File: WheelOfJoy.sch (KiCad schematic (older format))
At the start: 39 parts, among them CN1 JOY1, CN2 JOY2, CN3 JOY3, CN4 JOY4, CN5 JOY5, CN6 JOY6, CN7 JOY7, CN8 JOY8, CN9 DB15F, U1 CD4051B, U2 CD4051B, U3 CD4051B, U4 CD4051B, U5 CD4051B

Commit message: WIP
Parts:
- removed C4, C5: 100n, Capacitor_THT:C_Disc_D7.0mm_W2.5mm_P5.00mm, symbol Device:C
- removed CN5: JOY5, Connector_Dsub:DSUB-9_Male_EdgeMount_P2.77mm, symbol Connector:DB9_Male_MountingHoles
- removed CN6: JOY6, Connector_Dsub:DSUB-9_Male_EdgeMount_P2.77mm, symbol Connector:DB9_Male_MountingHoles
- removed CN7: JOY7, Connector_Dsub:DSUB-9_Male_EdgeMount_P2.77mm, symbol Connector:DB9_Male_MountingHoles
- removed CN8: JOY8, Connector_Dsub:DSUB-9_Male_EdgeMount_P2.77mm, symbol Connector:DB9_Male_MountingHoles
- removed RN1, RN2, RN3, RN4, RN5, RN6, RN7, RN8: 4.7k, Resistor_THT:R_Array_SIP6, symbol Device:R_Network05
- removed RN9: 100, Resistor_THT:R_Array_SIP10, symbol Device:R_Pack05_SIP_Split
- removed U1, U2, U3, U4, U5: CD4051B, Package_DIP:DIP-16_W7.62mm_Socket_LongPads, symbol Analog_Switch:CD4051B
- removed V6: PORT5_NO, WheelOfJoy:port5, symbol void:Void
- removed V7: PORT6_NO, WheelOfJoy:port6, symbol void:Void
- removed V8: PORT7_NO, WheelOfJoy:port7, symbol void:Void
- removed V9: PORT8_NO, WheelOfJoy:port8, symbol void:Void
- added RN1, RN2, RN3, RN4, RN5, RN6: 4.7k, Resistor_SMD:R_Array_Convex_4x0603, symbol Device:R_Pack04
- added RN7, RN8: 100, Resistor_SMD:R_Array_Convex_4x0603, symbol Device:R_Pack04_Split
- added U1, U2, U3: 74LS153, Package_SO:SOIC-16_3.9x9.9mm_P1.27mm, symbol 74xx:74LS153
- C1, C2, C3: footprint Capacitor_THT:C_Disc_D7.0mm_W2.5mm_P5.00mm -> Capacitor_SMD:C_0805_2012Metric_Pad1.18x1.45mm_HandSolder
- C6: footprint Capacitor_THT:CP_Radial_D6.3mm_P2.50mm -> Capacitor_SMD:C_1206_3216Metric_Pad1.33x1.80mm_HandSolder
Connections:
- net +5V: now also RN1.5 (R4.2), RN1.6 (R3.2), RN1.7 (R2.2), RN1.8 (R1.2), RN2.1 (R1.1), RN2.2 (R2.1), RN2.3 (R3.1), RN2.4 (R4.1), RN3.5 (R4.2), RN3.6 (R3.2), RN3.7 (R2.2), RN3.8 (R1.2), RN4.1 (R1.1), RN4.2 (R2.1), RN4.3 (R3.1), RN4.4 (R4.1), RN5.5 (R4.2), RN5.6 (R3.2), RN5.7 (R2.2), RN5.8 (R1.2), RN6.1 (R1.1), RN6.2 (R2.1), RN6.3 (R3.1), RN6.4 (R4.1), U1.16 (VCC), U2.16 (VCC), U3.16 (VCC)
- net GND: now also U1.1 (Ea), U1.15 (Eb), U1.8 (GND), U2.1 (Ea), U2.15 (Eb), U2.8 (GND), U3.1 (Ea), U3.15 (Eb), U3.8 (GND)
- net d0: now also RN8.5 (R4.2), U1.7 (Za)
- net d1: now also RN8.6 (R3.2), U1.9 (Zb)
- net d2: now also RN8.7 (R2.2), U2.7 (Za)
- net d3: now also RN8.8 (R1.2), U2.9 (Zb)
- net d4: now also RN7.5 (R4.2), U3.7 (Za)
- net d5: now also RN7.6 (R3.2), U3.9 (Zb); no longer CN9.11 (P111)
- net d6: now also U1.14 (S0), U2.14 (S0), U3.14 (S0)
- net d7: now also U1.2 (S1), U2.2 (S1), U3.2 (S1)
- net at CN4.4: now also RN3.1 (R1.1), U2.13 (I3b)
- net at CN1.4: now also RN3.4 (R4.1), U2.10 (I0b)
- net at CN2.4: now also RN3.3 (R3.1), U2.11 (I1b)
- net at CN3.4: now also RN3.2 (R2.1), U2.12 (I2b)
- net at CN4.6: now also RN6.8 (R1.2), U3.3 (I3a)
- net at CN1.6: now also RN6.5 (R4.2), U3.6 (I0a)
- net at CN2.6: now also RN6.6 (R3.2), U3.5 (I1a)
- net at CN3.6: now also RN6.7 (R2.2), U3.4 (I2a)
- net at CN4.1: now also RN2.8 (R1.2), U1.3 (I3a)
- net at CN1.1: now also RN2.5 (R4.2), U1.6 (I0a)
- net at CN2.1: now also RN2.6 (R3.2), U1.5 (I1a)
- net at CN3.1: now also RN2.7 (R2.2), U1.4 (I2a)
- net at CN1.3: now also RN4.5 (R4.2), U2.6 (I0a)
- net at CN1.2: now also RN1.4 (R4.1), U1.10 (I0b)
- net at CN1.9: now also RN5.4 (R4.1), U3.10 (I0b)
- net at CN2.3: now also RN4.6 (R3.2), U2.5 (I1a)
- net at CN2.2: now also RN1.3 (R3.1), U1.11 (I1b)
- net at CN2.9: now also RN5.3 (R3.1), U3.11 (I1b)
- net at CN3.3: now also RN4.7 (R2.2), U2.4 (I2a)
- net at CN3.2: now also RN1.2 (R2.1), U1.12 (I2b)
- net at CN3.9: now also RN5.2 (R2.1), U3.12 (I2b)
- net at CN4.3: now also RN4.8 (R1.2), U2.3 (I3a)
- net at CN4.2: now also RN1.1 (R1.1), U1.13 (I3b)
- net at CN4.9: now also RN5.1 (R1.1), U3.13 (I3b)
- net at CN9.10 (P10): now also RN7.4 (R4.1)
- net at CN9.2: now also RN8.4 (R4.1)
- net at CN9.3: now also RN8.3 (R3.1)
- net at CN9.4: now also RN8.2 (R2.1)
- net at CN9.5: now also RN8.1 (R1.1)
- new net: CN9.11 (P111), RN7.3 (R3.1)
- no-connect marks 11 -> 7
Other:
- note added: "SPARES"
- moved on the sheet: CN1, CN2, CN3, CN4, V0, V1, V2, V3, V4, V5

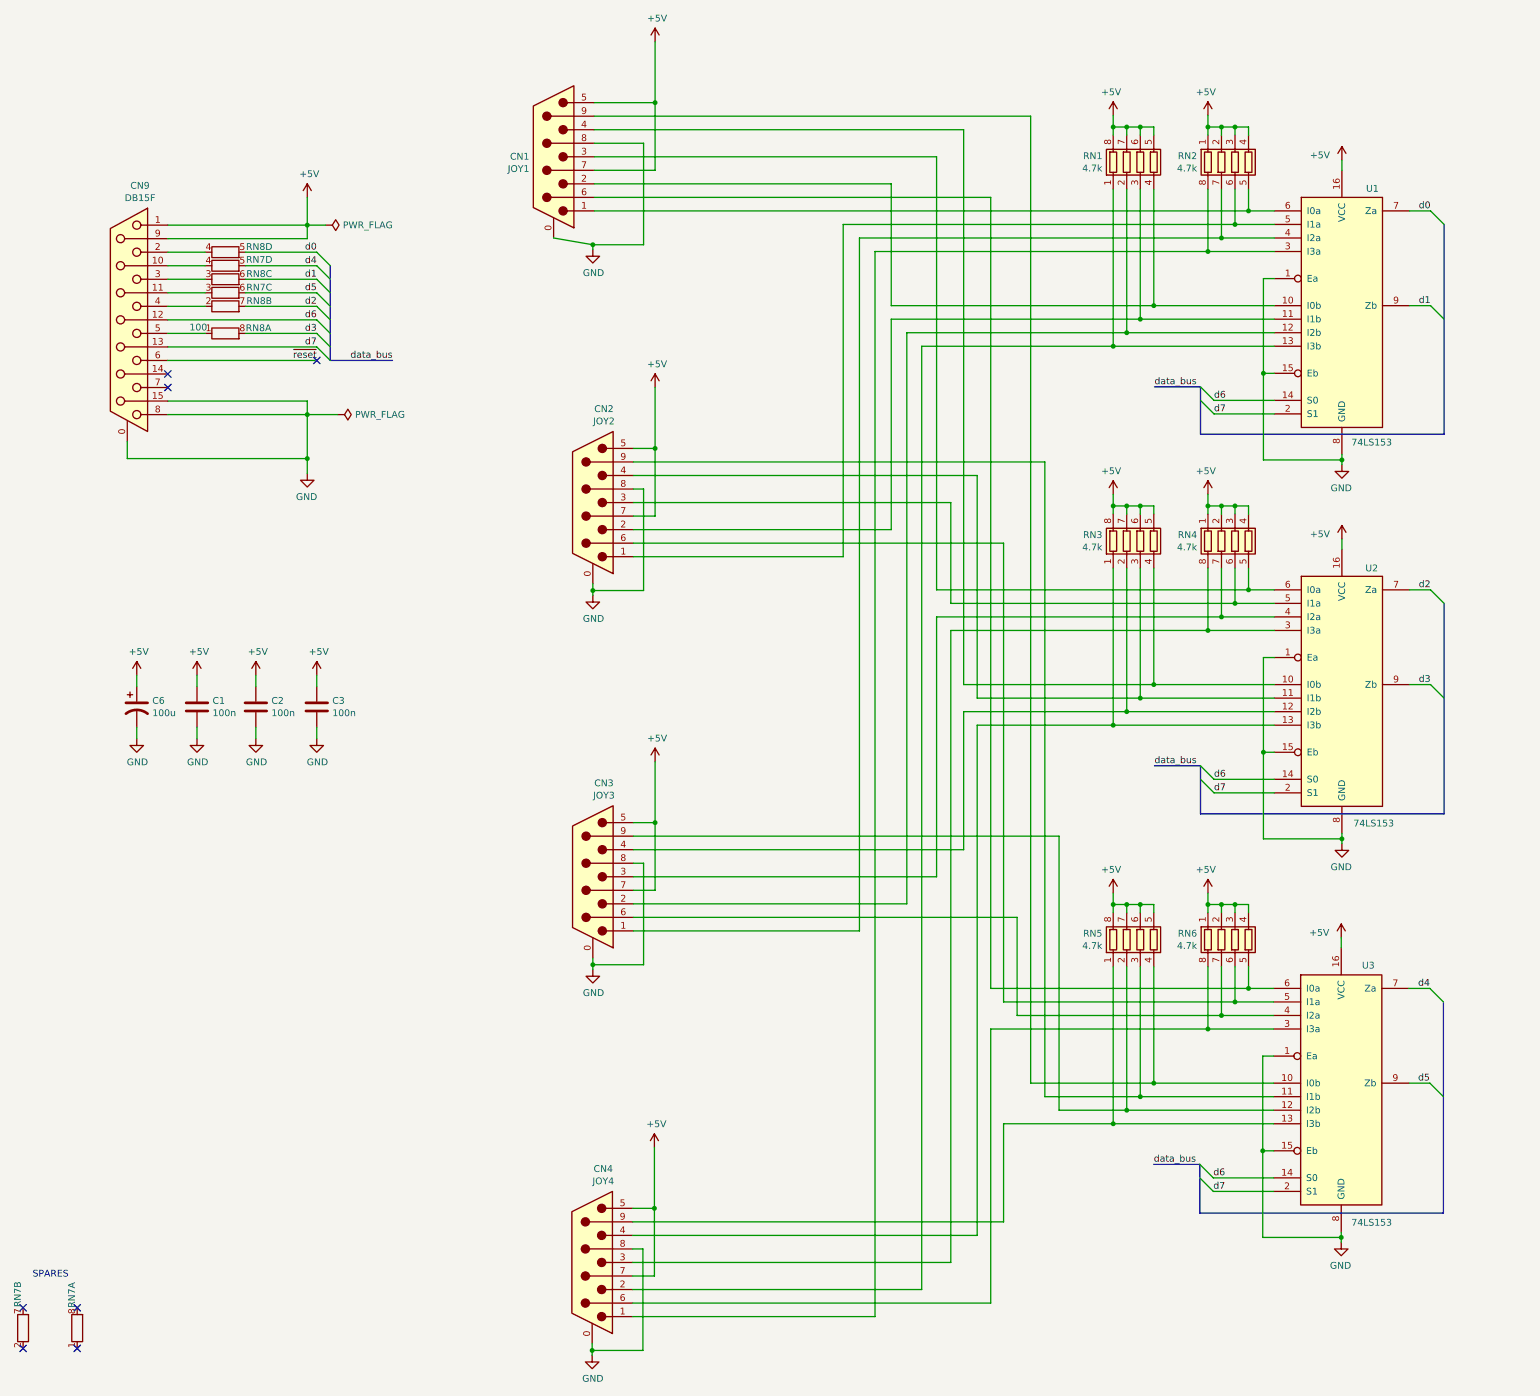
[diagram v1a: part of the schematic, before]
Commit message: Restart routing from scratch
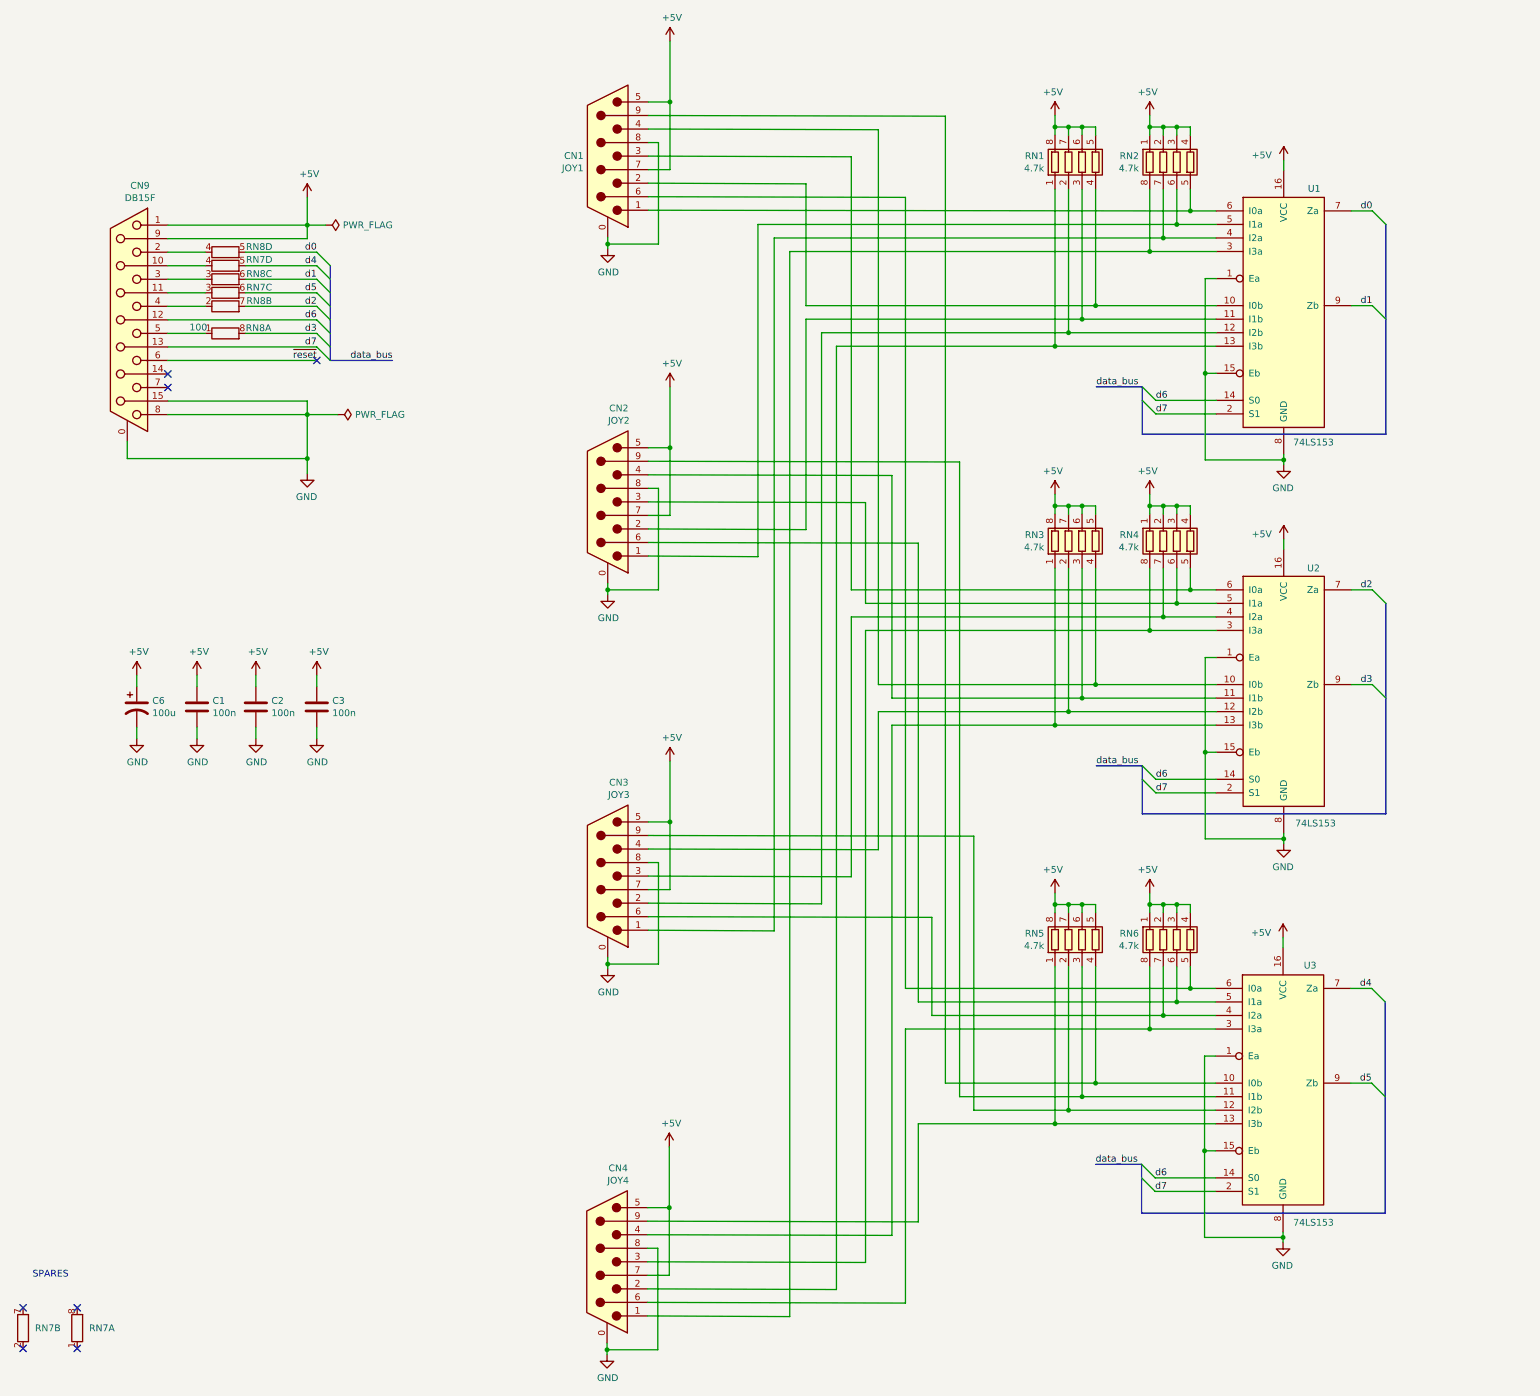
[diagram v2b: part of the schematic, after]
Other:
- moved on the sheet: CN1, CN2, CN3, CN4, RN1, RN2, RN3, RN4, RN5, RN6, U1, U2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

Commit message: Honing tracks
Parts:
- renumbered C6 to C4
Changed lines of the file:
@@
 $EndComp
 $Comp
-L Device:CP1 C6
+L Device:CP1 C4
 U 1 1 63690C73
 P 1985 5885
-F 0 "C6" H 2100 5931 50  0000 L CNN
+F 0 "C4" H 2100 5931 50  0000 L CNN
 F 1 "100u" H 2100 5840 50  0000 L CNN
 F 2 "Capacitor_SMD:C_1206_3216Metric_Pad1.33x1.80mm_HandSolder" H 1985 5885 50  0001 C CNN
@@
 Wire Wire Line
 	9770 2060 9770 2220
+Connection ~ 9770 2220
+Wire Wire Line
+	9770 2220 9960 2220
 Wire Bus Line
 	11215 5120 11215 6675
@@
 Wire Bus Line
 	3415 2625 3415 3325
-Connection ~ 9770 2220
-Wire Wire Line
-	9770 2220 9960 2220
 $EndSCHEMATC

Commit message: Almost there
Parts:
- renumbered CN9 to CN5
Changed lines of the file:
@@
 $EndComp
 $Comp
-L Connector:DB15_Female_MountingHoles CN9
+L Connector:DB15_Female_MountingHoles CN5
 U 1 1 636CDFF8
 P 1915 3025
-F 0 "CN9" H 1821 4017 50  0000 C CNN
+F 0 "CN5" H 1821 4017 50  0000 C CNN
 F 1 "DB15F" H 1821 3926 50  0000 C CNN
 F 2 "Connector_Dsub:DSUB-15_Female_EdgeMount_P2.77mm" H 1915 3025 50  0001 C CNN

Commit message: YEAH!
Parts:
- C4: footprint Capacitor_SMD:C_1206_3216Metric_Pad1.33x1.80mm_HandSolder -> Capacitor_Tantalum_SMD:CP_EIA-7343-30_AVX-N_Pad2.25x2.55mm_HandSolder
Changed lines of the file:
@@
 F 0 "C4" H 2100 5931 50  0000 L CNN
 F 1 "100u" H 2100 5840 50  0000 L CNN
-F 2 "Capacitor_SMD:C_1206_3216Metric_Pad1.33x1.80mm_HandSolder" H 1985 5885 50  0001 C CNN
+F 2 "Capacitor_Tantalum_SMD:CP_EIA-7343-30_AVX-N_Pad2.25x2.55mm_HandSolder" H 1985 5885 50  0001 C CNN
 F 3 "~" H 1985 5885 50  0001 C CNN
 	1    1985 5885
